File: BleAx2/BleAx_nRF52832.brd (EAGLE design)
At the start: 55.7 x 22.9 mm, 60 parts, among them CN1 6p-2.54, J1 2.0MM-90D, J5 MICROUSB, U1 NRF52832, U2 MCP73832T-2ACI/OT-SOT23-5, U4 MIC5225-3.3, X1 32MHz, X2 32.768kHz

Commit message: last today
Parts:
- removed U$10, U$9: 1,1/0,6, wirepad:1,1/0,6
- removed X1: 32MHz, Nordic_nRF:BT-XTAL_2016_N
- added Q1: 32MHz, crystal:HC49/S
- added Q2: 32MHz, crystal-geyer_V1_0:5.0X3.2_KX-9A
- added Q3: (no value), crystal:TC38H
- moved U$17 197.8 mm to (37.2, 6.00), turned to 90 degrees
- moved U$16 185.5 mm to (36.6, 4.60), turned to 90 degrees
- moved U$15 175.7 mm to (35.4, 6.00), turned to 90 degrees
- moved U$14 161.9 mm to (36.0, 2.80), turned to 90 degrees
- moved U$13 150.6 mm to (38.0, 1.70), turned to 90 degrees
- moved U$12 147.8 mm to (42.2, 8.60), turned to 90 degrees
- moved U$11 138.0 mm to (44.5, 8.60), turned to 90 degrees
- moved U$8 104.1 mm to (28.1, 11.6)
- moved U$7 94.7 mm to (29.3, 12.4)
- moved U$6 82.8 mm to (29.3, 10.8)
- moved U$5 71.4 mm to (28.1, 10.0)
- moved U$4 61.4 mm to (29.3, 9.20)
- moved U$3 50.8 mm to (28.1, 8.40)
- moved R3 30.1 mm to (5.50, 3.40), turned to 180 degrees
- moved D4 23.3 mm to (2.80, 3.40), turned to 180 degrees
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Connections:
- removed net GND@2: U3.12
- removed net VCC: U3.14
- new net N$15: U$7.P$1, U1.4
- new net N$16: U$8.P$1, U1.5
- net GND: now also U3.10, U3.12; no longer X1.2, X1.4
- net N$3: now also Q1.2, Q2.3; no longer X1.3
- net VDD_P3V3: now also U3.14
- net X1: now also Q1.1, Q2.1; no longer X1.1
- net XL1: now also Q3.1
- net XL2: now also Q3.2
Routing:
- net VDD_P3V3: track 44.0 -> 132.5 mm, vias 4 -> 5
- net LED_01: track 0.00 -> 53.7 mm, vias 0 -> 2
- net LED_02: track 0.00 -> 51.0 mm
- net VDD_BATT: track 1.40 -> 39.9 mm
- net MISO_01: track 0.00 -> 30.7 mm, vias 0 -> 2
- net LIS_CS: track 0.00 -> 25.1 mm, vias 0 -> 1
- net MOSI_01: track 0.00 -> 24.6 mm
- net SST26_CE: track 0.00 -> 18.1 mm, vias 0 -> 1
- net VCC_P5V0_USB: track 0.00 -> 15.8 mm, vias 0 -> 1
- net MISO_02: track 0.00 -> 15.3 mm, vias 0 -> 1
- net MOSI_02: track 0.00 -> 15.1 mm, vias 0 -> 1
- net SCK_02: track 0.00 -> 9.40 mm, vias 0 -> 1
- net N$10: track 0.00 -> 8.94 mm, vias 0 -> 1
- net N$14: track 0.00 -> 7.33 mm
- net N$13: track 0.00 -> 6.95 mm, vias 0 -> 1
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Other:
- board size 55.7 x 22.9 mm -> 51.7 x 22.9 mm

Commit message: size decrise
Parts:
- removed U$1, U$11, U$12, U$13, U$14, U$15, U$16, U$17, U$3, U$4, U$5, U$6, U$7, U$8: 1,1/0,6, wirepad:1,1/0,6
- moved D4 20.0 mm to (13.8, 20.1)
- moved R3 19.8 mm to (16.2, 20.1)
- moved U$2 19.7 mm to (22.9, 5.05)
- moved C2 18.9 mm to (26.7, 15.7), flipped to the bottom, turned to 0 degrees
- moved D1 17.9 mm to (13.8, 19.0)
- moved R2 17.7 mm to (16.2, 19.0)
- moved BTN1 17.4 mm to (8.40, 5.70)
- moved C5 15.9 mm to (18.5, 8.40), turned to 180.1 degrees
- moved Q1 15.4 mm to (27.4, 17.6), turned to 129.4 degrees
- moved Q2 15.4 mm to (27.4, 17.6)
- moved D3 14.9 mm to (4.80, 21.0)
- moved C1 14.7 mm to (25.7, 17.7), flipped to the bottom, turned to 0 degrees
- moved C18 14.2 mm to (19.0, 12.2)
- moved U1 14.2 mm to (23.1, 11.4)
- moved R8 14.2 mm to (5.60, 10.1)
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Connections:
- removed net N$13: U$12.P$1, U1.19
- removed net N$14: U$13.P$1, U1.20
- removed net N$15: U$7.P$1, U1.4
- removed net N$16: U$8.P$1, U1.5
- removed net N$8: U$11.P$1, U1.18
- net LIS_CS: no longer U$3.P$1
- net LIS_INT1: no longer U$1.P$1
- net MISO_01: no longer U$4.P$1
- net MISO_02: now also U1.14; no longer U$14.P$1, U1.15
- net MOSI_01: no longer U$5.P$1
- net MOSI_02: no longer U$16.P$1
- net SCK_01: no longer U$6.P$1
- net SCK_02: no longer U$17.P$1
- net SST26_CE: now also U1.15; no longer U$15.P$1, U1.14
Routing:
- net VDD_P3V3: track 132.5 -> 14.7 mm, vias 5 -> 3
- net LED_01: track 53.7 -> 0.00 mm, vias 2 -> 0
- net LED_02: track 51.0 -> 0.00 mm
- net VDD_BATT: track 39.9 -> 0.00 mm
- net P0.21/RESET: track 34.2 -> 0.00 mm, vias 1 -> 0
- net MISO_01: track 30.7 -> 0.00 mm, vias 2 -> 0
- net LIS_CS: track 25.1 -> 0.00 mm, vias 1 -> 0
- net MOSI_01: track 24.6 -> 0.00 mm
- net SST26_CE: track 18.1 -> 0.00 mm, vias 1 -> 0
- net VCC_P5V0_USB: track 15.8 -> 0.00 mm, vias 1 -> 0
- net MISO_02: track 15.3 -> 0.00 mm, vias 1 -> 0
- net MOSI_02: track 15.1 -> 0.00 mm, vias 1 -> 0
- net XL1: track 11.0 -> 0.00 mm
- net N$7: track 9.54 -> 0.00 mm
- net SCK_02: track 9.40 -> 0.00 mm, vias 1 -> 0
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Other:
- board size 51.7 x 22.9 mm -> 37.5 x 22.9 mm

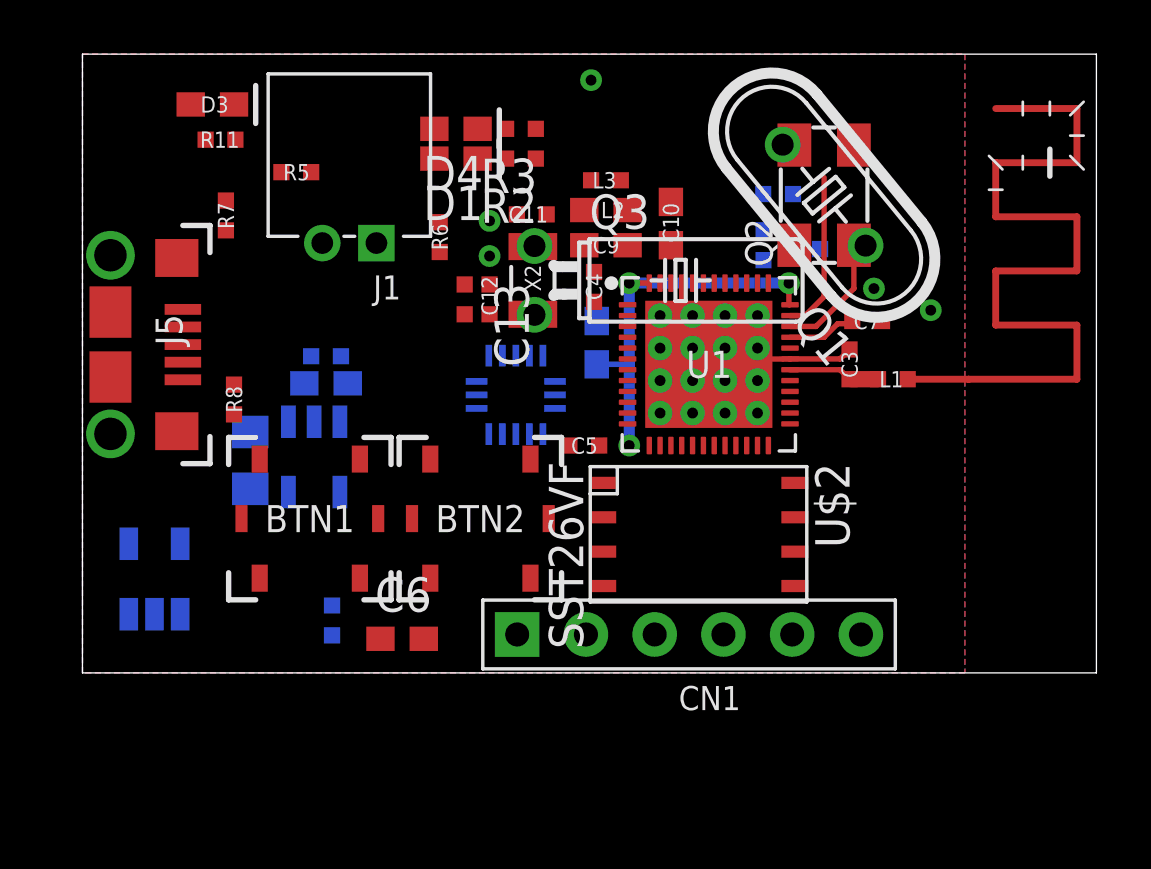
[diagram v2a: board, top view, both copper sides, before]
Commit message: размеры уменьшил
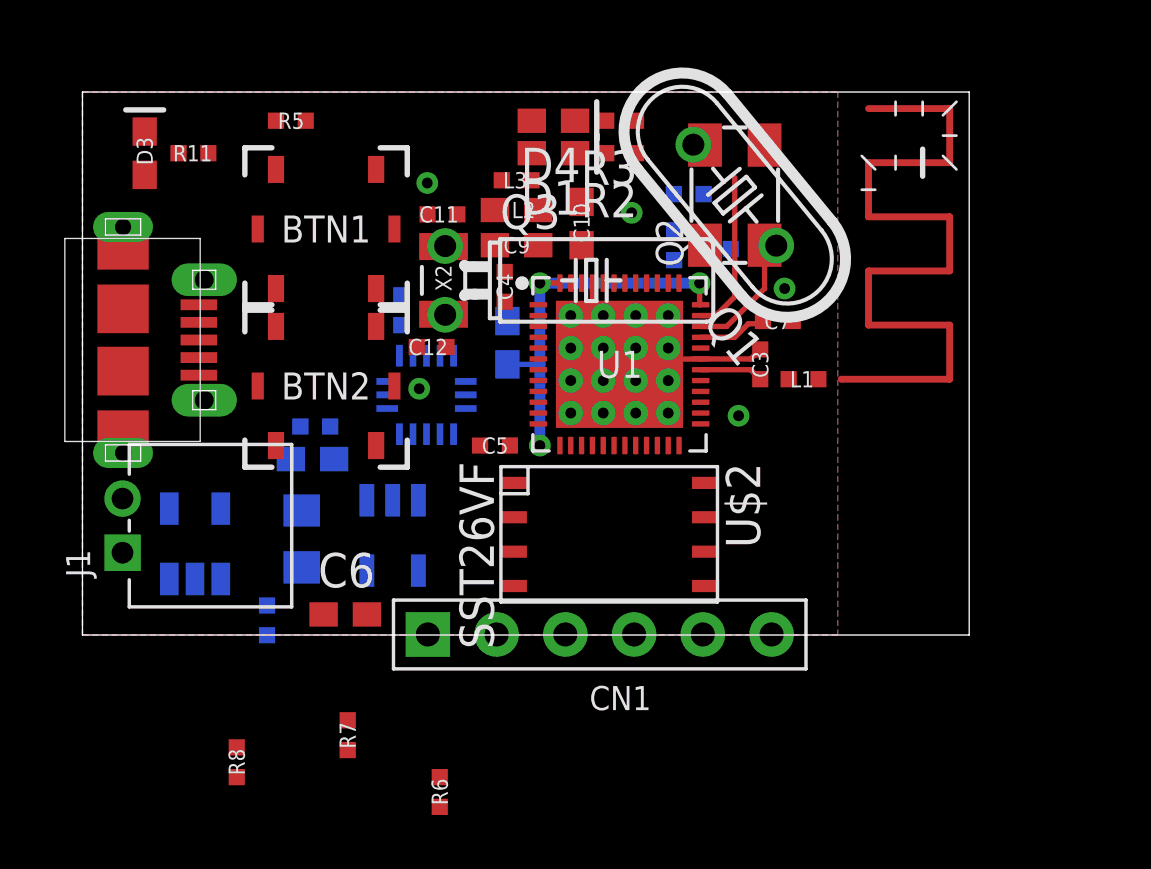
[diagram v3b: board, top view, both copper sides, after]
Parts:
- removed J5: MICROUSB, Nordic_misc:USB-MICRO-B-RA-SMD-PIP
- added U$1: MICRO-USB-RECEPTACLE47589-0001, con-molex-usb:47589-0001
- moved R6 20.5 mm to (13.2, -4.40)
- moved R7 19.7 mm to (9.80, -2.30)
- moved J1 14.6 mm to (4.73, 5.44), turned to 90 degrees
- moved R8 13.4 mm to (5.70, -3.30)
- moved BTN1 10.7 mm to (9.00, 16.4)
- moved BTN2 7.52 mm to (9.00, 10.6)
- moved ANT1 4.70 mm to (28.0, 10.8)
- moved U4 4.10 mm to (11.5, 5.08)
- moved R3 3.71 mm to (19.9, 20.4)
- moved R2 3.71 mm to (19.9, 19.2)
- moved D4 3.61 mm to (17.4, 20.4)
- moved D1 3.61 mm to (17.4, 19.2)
- moved C19 3.47 mm to (8.10, 5.00)
- moved C1 3.30 mm to (22.4, 17.7)
- moved C11 3.30 mm to (13.3, 16.9)
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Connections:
- net GND: now also U$1.5; no longer J5.5
- net VCC_P5V0_USB: now also U$1.1; no longer J5.1
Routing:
- net N$5: track 2.25 -> 0.00 mm
- net ANT: track 3.39 -> 2.34 mm
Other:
- board size 37.5 x 22.9 mm -> 32.8 x 20.1 mm

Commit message: evolv
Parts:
- removed Q1: 32MHz, crystal:HC49/S
- removed Q3: (no value), crystal:TC38H
- moved C1 1.40 mm to (22.4, 16.3)
- moved C10 1.40 mm to (18.4, 15.2)
- moved C11 1.40 mm to (13.3, 15.5)
- moved L2 1.40 mm to (16.0, 15.7)
- moved ANT1 1.40 mm to (28.0, 9.45)
- moved BTN2 1.40 mm to (9.00, 9.20)
- moved C13 1.40 mm to (11.8, 12.0)
- moved C17 1.40 mm to (8.50, 6.50)
- moved C2 1.40 mm to (23.4, 14.3)
- moved C3 1.40 mm to (25.0, 10.0)
- moved C4 1.40 mm to (15.6, 12.9)
- moved C5 1.40 mm to (15.2, 7.00)
- moved C7 1.40 mm to (25.7, 11.6)
- moved C8 1.40 mm to (21.9, 14.4)
- moved C9 1.40 mm to (16.0, 14.4)
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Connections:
- net N$3: no longer Q1.2
- net X1: no longer Q1.1
- net XL1: no longer Q3.1
- net XL2: no longer Q3.2
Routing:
- net N$3: track 6.65 -> 5.95 mm

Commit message: evolve
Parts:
- removed Q2: 32MHz, crystal-geyer_V1_0:5.0X3.2_KX-9A
- added X1: FA-128, crystals:FA-128
- C1, C2: value 12pF -> 10pF
- moved R7 22.6 mm to (4.80, 18.3)
- moved R6 12.5 mm to (22.7, 2.40)
- moved R8 10.7 mm to (4.90, 6.00)
- moved U2 7.58 mm to (5.26, 10.9)
- moved BTN2 4.93 mm to (8.50, 4.30)
- moved R5 4.65 mm to (12.3, 18.3)
- moved D4 4.05 mm to (21.2, 17.6), turned to 0 degrees
- moved D1 3.96 mm to (21.2, 18.9), turned to 0 degrees
- moved C4 3.47 mm to (12.7, 14.8)
- moved R3 2.86 mm to (20.5, 16.2), turned to 90 degrees
- moved ANT1 2.80 mm to (25.2, 9.45)
- moved C3 2.80 mm to (22.2, 10.0)
- moved C5 2.80 mm to (12.4, 7.00)
- moved C6 2.80 mm to (6.91, 0.76)
- moved C7 2.80 mm to (22.9, 11.6)
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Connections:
- net GND: now also X1.2, X1.4
- net MISO_02: now also U1.15; no longer U1.14
- net N$3: now also X1.3; no longer Q2.3
- net SST26_CE: now also U1.14; no longer U1.15
- net X1: now also X1.1; no longer Q2.1
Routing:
- net VDD_P3V3: track 14.7 -> 84.0 mm, vias 3 -> 4
- net N$6: track 0.00 -> 20.8 mm, vias 0 -> 2
- net VDD_BATT: track 0.00 -> 20.8 mm, vias 0 -> 2
- net N$1: track 0.00 -> 19.3 mm
- net N$7: track 0.00 -> 12.0 mm
- net N$10: track 0.00 -> 9.52 mm, vias 0 -> 1
- net P0.18/SWO: track 0.00 -> 8.45 mm, vias 0 -> 1
- net MOSI_02: track 0.00 -> 7.30 mm
- net SCK_02: track 0.00 -> 6.01 mm
- net LED_02: track 0.00 -> 4.83 mm
- net LED_01: track 0.00 -> 4.33 mm
- net MISO_02: track 0.00 -> 4.30 mm
- net DEC4: track 0.00 -> 4.18 mm
- net GND: track 23.9 -> 27.0 mm
- net SST26_CE: track 0.00 -> 2.98 mm
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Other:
- board size 32.8 x 20.1 mm -> 30 x 20.1 mm

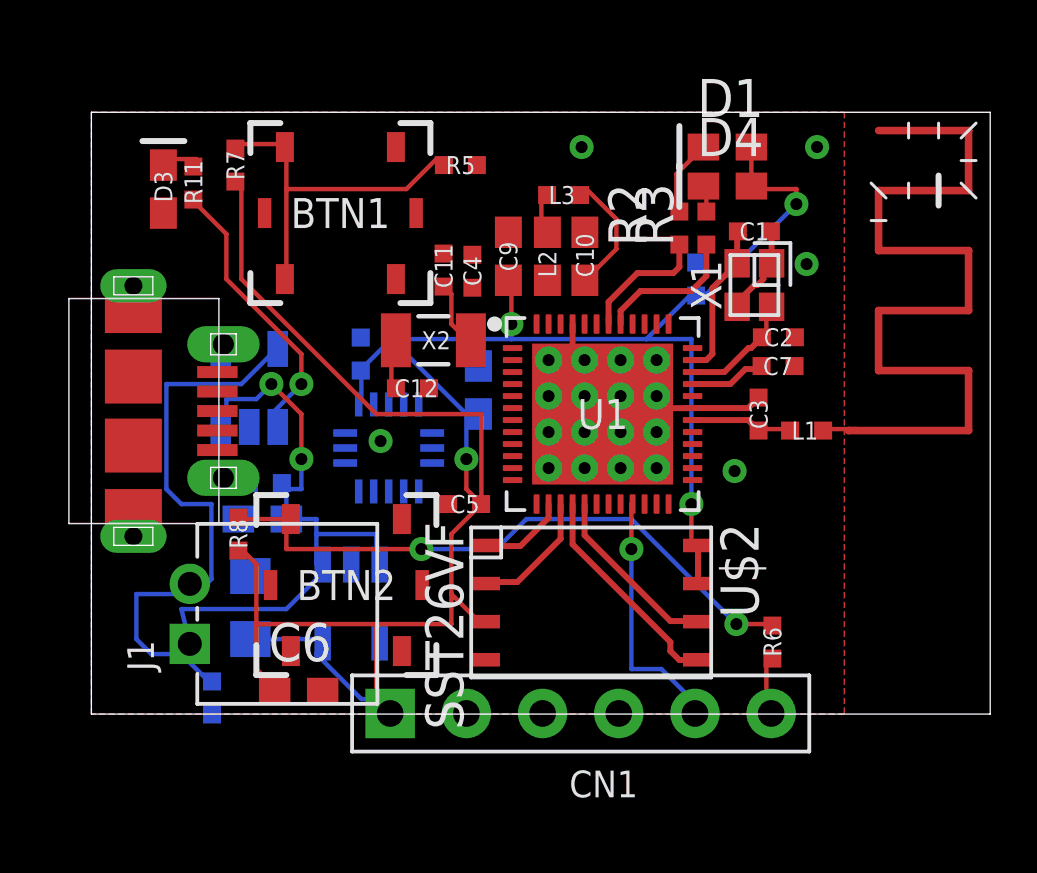
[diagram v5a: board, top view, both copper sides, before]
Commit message: button del
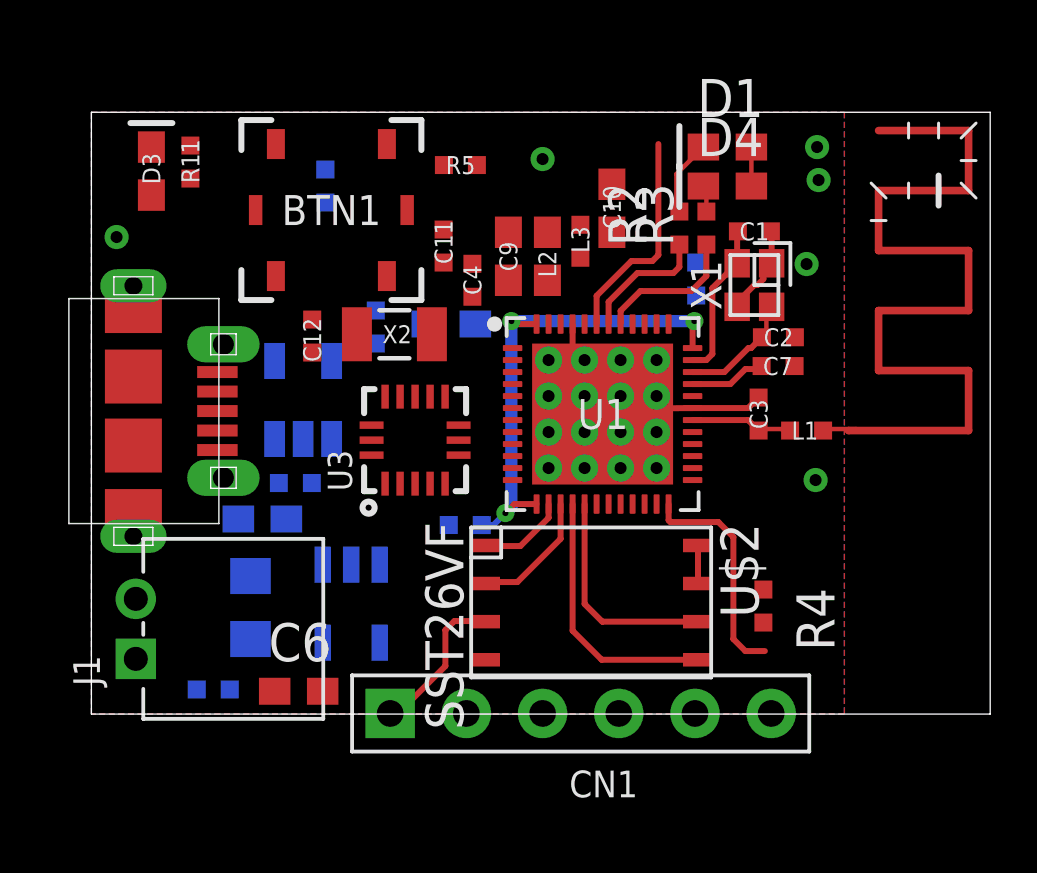
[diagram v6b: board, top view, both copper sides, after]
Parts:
- removed BTN2: PANASONIC_EVQPT5A15, Nordic_misc:PANASONIC_EVQPT5A15
- removed R6: 330R, Nordic_misc:RESC0402_N
- removed R8: 100k, Nordic_misc:RESC0402_N
- added R4: 100k, Nordic_misc:RESC0402_N
- moved C12 3.77 mm to (7.36, 12.6), turned to 90 degrees
- moved R7 3.08 mm to (7.80, 17.6), flipped to the bottom
- moved C18 2.38 mm to (12.0, 13.0), turned to 0 degrees
- moved J1 1.87 mm to (4.73, 2.84)
- moved U2 1.84 mm to (7.06, 10.5)
- moved C10 1.84 mm to (17.4, 16.9)
- moved L3 1.64 mm to (16.3, 15.8), turned to 270 degrees
- moved X2 1.32 mm to (10.1, 12.7)
- moved C13 1.03 mm to (9.48, 12.9)
- moved C16 1.00 mm to (6.80, 7.70)
- moved U3 0.92 mm to (10.8, 9.13), flipped to the top, turned to 90 degrees
- moved C11 0.80 mm to (11.7, 15.6)
- moved D3 0.72 mm to (2.00, 18.1)
- moved R11 0.71 mm to (3.30, 18.4)
- moved C5 0.70 mm to (12.5, 6.30), flipped to the bottom, turned to 0.1 degrees
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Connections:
- removed net N$6: BTN2.1, R6.2, R8.1
- new net VCC: R4.1
- net GND: no longer BTN2.3, BTN2.4, BTN2.5, BTN2.6
- net LIS_CS: now also U1.6; no longer U1.11
- net LIS_INT1: now also U1.5; no longer U1.12
- net MISO_01: now also U1.8; no longer U1.10
- net P0.21/RESET: now also R4.2; no longer R6.1
- net SCK_01: now also U1.10; no longer U1.8
- net VDD_P3V3: no longer R8.2
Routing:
- net VDD_P3V3: track 84.0 -> 24.2 mm, vias 4 -> 3
- net N$6: track 20.8 -> 0.00 mm, vias 2 -> 0
- net VDD_BATT: track 20.8 -> 0.00 mm, vias 2 -> 0
- net N$1: track 19.3 -> 0.00 mm
- net N$7: track 12.0 -> 0.00 mm
- net N$10: track 9.52 -> 0.00 mm, vias 1 -> 0
- net P0.18/SWO: track 8.45 -> 0.00 mm, vias 1 -> 0
- net BTTN_01: track 0.00 -> 7.26 mm
- net P0.21/RESET: track 2.26 -> 8.05 mm
- net DEC4: track 4.18 -> 0.00 mm
- net XL1: track 2.22 -> 0.00 mm
- net N$2: track 1.76 -> 0.00 mm
- net XL2: track 1.69 -> 0.00 mm
- net MOSI_02: track 7.30 -> 8.80 mm
- net N$9: track 1.49 -> 0.00 mm
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
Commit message: evolve
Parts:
- removed BTN1: PANASONIC_EVQPT5A15, Nordic_misc:PANASONIC_EVQPT5A15
- removed R5: 330R, Nordic_misc:RESC0402_N
- removed R7: 100k, Nordic_misc:RESC0402_N
- added BTN2: PANASONIC_EVQPT5A15, Nordic_misc:PANASONIC_EVQPT5A15
- added R6: 100k, Nordic_misc:RESC0402_N
- added R8: 330R, Nordic_misc:RESC0402_N
- moved R1 13.9 mm to (3.72, 14.7), turned to 270 degrees
- moved U2 6.15 mm to (6.04, 16.5), turned to 180 degrees
- moved C17 3.64 mm to (4.70, 3.00), flipped to the top, turned to 90 degrees
- moved D1 3.10 mm to (24.1, 17.8), turned to 90 degrees
- moved C6 2.29 mm to (7.34, 3.01), flipped to the bottom, turned to 90 degrees
- moved C1 1.41 mm to (22.3, 17.5)
- moved C10 1.22 mm to (18.1, 17.9)
- moved X1 1.22 mm to (22.3, 15.5)
- moved U3 1.20 mm to (9.59, 9.03)
- moved U4 1.20 mm to (9.86, 3.78)
- moved L3 1.12 mm to (16.8, 16.8)
- moved C5 1.12 mm to (13.5, 6.80)
- moved D4 1.12 mm to (21.4, 18.7), turned to 180 degrees
- moved L2 1.04 mm to (15.5, 16.3)
- moved C9 1.00 mm to (14.0, 16.3)
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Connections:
- removed net N$11: D1.1, R2.2
- removed net N$12: D4.1, R3.2
- removed net VCC: R4.1
- new net N$6: BTN2.1, BTN2.2, R6.1, R8.2
- new net N$8: D4.2, R3.2
- net BTTN_01: now also R8.1; no longer R5.1
- net GND: now also BTN2.3, BTN2.4, BTN2.5, BTN2.6, D1.1, D4.1; no longer BTN1.3, BTN1.4, BTN1.5, BTN1.6
- net N$7: now also D1.2, R2.2; no longer BTN1.1, BTN1.2, R5.2, R7.1
- net VDD_P3V3: now also R4.1, R6.2; no longer D1.2, D4.2, R7.2
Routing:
- net SWDIO: track 0.00 -> 18.6 mm, vias 0 -> 1
- net SWDCLK: track 0.00 -> 14.7 mm, vias 0 -> 1
- net P0.18/SWO: track 0.00 -> 9.45 mm, vias 0 -> 1
- net GND: track 27.0 -> 35.1 mm, vias 6 -> 9
- net P0.21/RESET: track 8.05 -> 11.1 mm
- net N$11: track 2.54 -> 0.00 mm, vias 0 -> 1
- net VDD_P3V3: track 24.2 -> 22.3 mm, vias 3 -> 4
- net LED_02: track 4.83 -> 3.07 mm
- net SCK_02: track 7.35 -> 9.06 mm
- net SST26_CE: track 2.98 -> 4.50 mm
- net N$5: track 1.39 -> 0.00 mm
- net ANT: track 3.40 -> 2.34 mm
- net LED_01: track 4.33 -> 3.30 mm
- net MOSI_02: track 8.80 -> 9.80 mm
- net MISO_02: track 4.30 -> 5.30 mm
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
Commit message: willl be think this is start point
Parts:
- moved BTN2 1.00 mm to (7.90, 16.9)
- moved C5 0.67 mm to (13.2, 7.40)
- moved U4 0.40 mm to (10.3, 3.78)
- moved X2 0.40 mm to (10.1, 12.6)
- moved C11 0.20 mm to (11.5, 16.6)
- moved C12 0.20 mm to (7.46, 12.7)
- moved U$2 0.20 mm to (16.9, 3.85)
- moved ANT1 0.14 mm to (25.0, 9.45)
- moved R2 0.10 mm to (19.5, 16.9)
- moved R3 0.10 mm to (20.5, 16.9)
- moved R8 0.10 mm to (13.6, 19.3)
- renumbered U3 to U$3
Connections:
- net LIS_CS: now also U1.9; no longer U1.6
- net LIS_INT1: now also U1.8; no longer U1.5
- net MISO_01: now also U1.10; no longer U1.8
- net MOSI_01: now also U1.11; no longer U1.9
- net SCK_01: now also U1.12; no longer U1.10
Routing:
- net GND: track 35.1 -> 1.13 mm, vias 9 -> 0
- net VDD_BATT: track 0.00 -> 28.3 mm, vias 0 -> 1
- net VDD_P3V3: track 22.3 -> 46.2 mm, vias 4 -> 0
- net SWDIO: track 18.6 -> 0.00 mm, vias 1 -> 0
- net SWDCLK: track 14.7 -> 0.00 mm, vias 1 -> 0
- net MOSI_02: track 9.80 -> 0.00 mm
- net P0.18/SWO: track 9.45 -> 0.00 mm, vias 1 -> 0
- net SCK_02: track 9.06 -> 0.00 mm
- net N$6: track 0.00 -> 8.59 mm
- net P0.21/RESET: track 11.1 -> 3.48 mm
- net VCC_P5V0_USB: track 0.00 -> 7.60 mm, vias 0 -> 1
- net N$7: track 0.00 -> 6.88 mm
- net BTTN_01: track 6.86 -> 0.00 mm
- net MISO_02: track 5.30 -> 0.00 mm
- net SST26_CE: track 4.50 -> 0.00 mm
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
